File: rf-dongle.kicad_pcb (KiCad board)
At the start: 4 copper layers, 33 x 18 mm, 35 parts, among them J1 USB_A, J3 TC2030, SW1 SW_Push, SW2 SW_Push, U1 nRF52840-QIXX, X1 32MHz, X2 32.768kHz

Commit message: before new programming pins
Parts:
- added H1: VBUS, TestPoint:TestPoint_THTPad_D1.0mm_Drill0.5mm, F.Cu at (57.6, 41.6)
- added H2: VEXT, TestPoint:TestPoint_THTPad_D1.0mm_Drill0.5mm, F.Cu at (57.6, 44.6)
- added H3: SWDIO, TestPoint:TestPoint_THTPad_D1.0mm_Drill0.5mm, F.Cu at (57.6, 47.7)
- added H4: SWDCLK, TestPoint:TestPoint_THTPad_D1.0mm_Drill0.5mm, F.Cu at (57.6, 50.8)
- added H5: GND, TestPoint:TestPoint_THTPad_D1.0mm_Drill0.5mm, F.Cu at (57.8, 53.4)
- moved X1 0.08 mm to (46.5, 40.6)
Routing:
- net SWDIO: track 19.9 -> 20.5 mm
- net GND: track 26.6 -> 26.7 mm, vias 55 -> 54
- net D-: vias 1 -> 0
- net D+: vias 1 -> 0

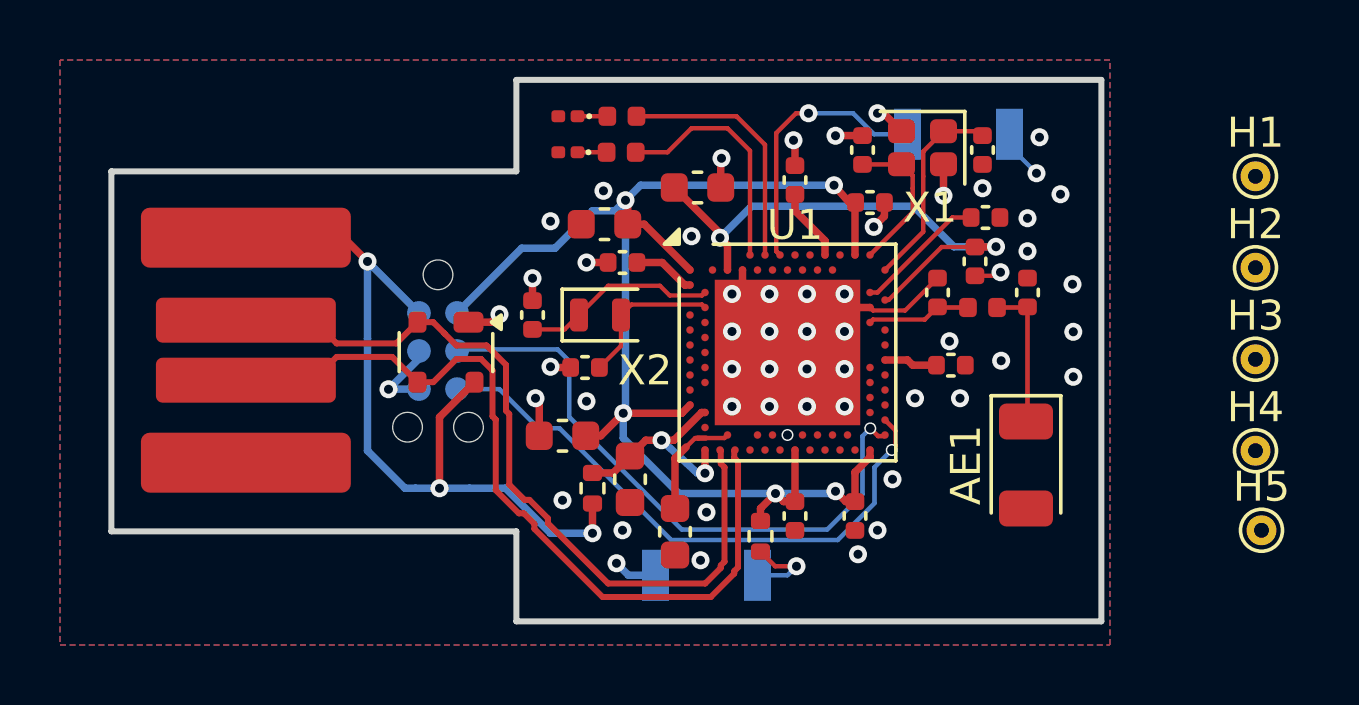
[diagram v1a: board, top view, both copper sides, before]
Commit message: rework programming pins, cleanup pcb routing
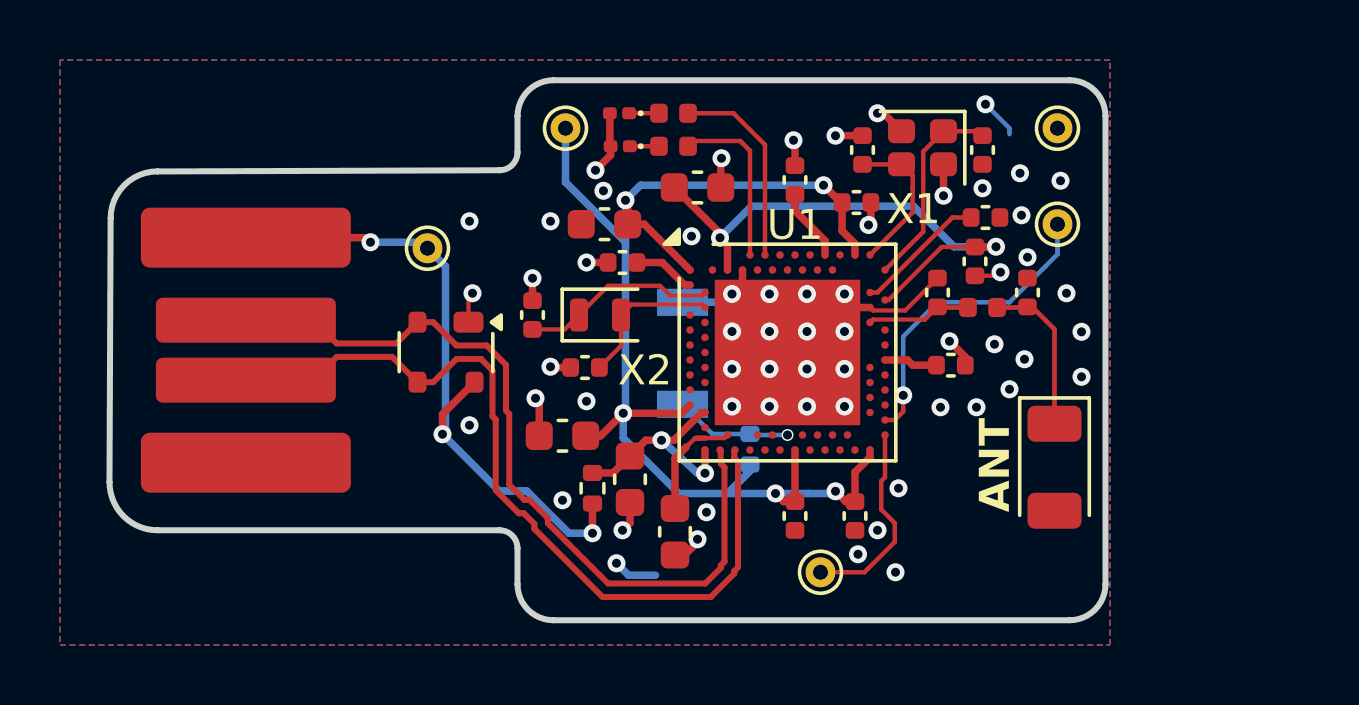
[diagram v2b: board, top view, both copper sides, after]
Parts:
- removed J3: TC2030, Connector:Tag-Connect_TC2030-IDC-NL_2x03_P1.27mm_Vertical
- removed SW2: SW_Push, Button_Switch_SMD:SW_SPST_B3U-1000P
- R2: moved to B.Cu
- moved H1 27.7 mm to (30.0, 44.0)
- moved H2 23.5 mm to (34.6, 40.0)
- moved H3 16.1 mm to (43.1, 54.8)
- moved H5 15.0 mm to (51.0, 40.0)
- moved H4 10.0 mm to (51.0, 43.2)
- moved SW1 7.44 mm to (38.5, 47.5), turned to -90 degrees
- moved R2 2.92 mm to (40.8, 50.7), turned to 90 degrees
- moved D3 1.76 mm to (38.2, 40.6)
- moved R4 1.76 mm to (36.4, 40.6)
- moved D2 1.72 mm to (38.2, 39.5)
- moved R3 1.72 mm to (36.4, 39.5)
- moved AE1 0.95 mm to (50.9, 51.3)
- moved C12 0.45 mm to (44.3, 42.5)
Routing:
- net SWDIO: track 20.5 -> 6.75 mm, vias 1 -> 0
- net BTN_1: track 9.06 -> 0.00 mm, vias 1 -> 0
- net SWDCLK: track 19.7 -> 10.7 mm
- net VBUS: track 26.8 -> 22.2 mm
- net RESET: track 8.15 -> 3.92 mm, vias 2 -> 1
- net GND: track 26.7 -> 30.3 mm, vias 54 -> 59
- net VEXT: track 46.8 -> 44.0 mm
- net LED_2: track 7.93 -> 5.75 mm
- net LED_1: track 8.35 -> 6.67 mm
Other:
- board size 33 x 18 mm -> 33.2 x 18 mm
- board text added: "ANT"
- board text added: "GND"
- board text added: "RESET"
- board text added: "SWDCLK"
- board text added: "SWDIO"
- board text added: "VBUS"
- board text added: "VEXT"

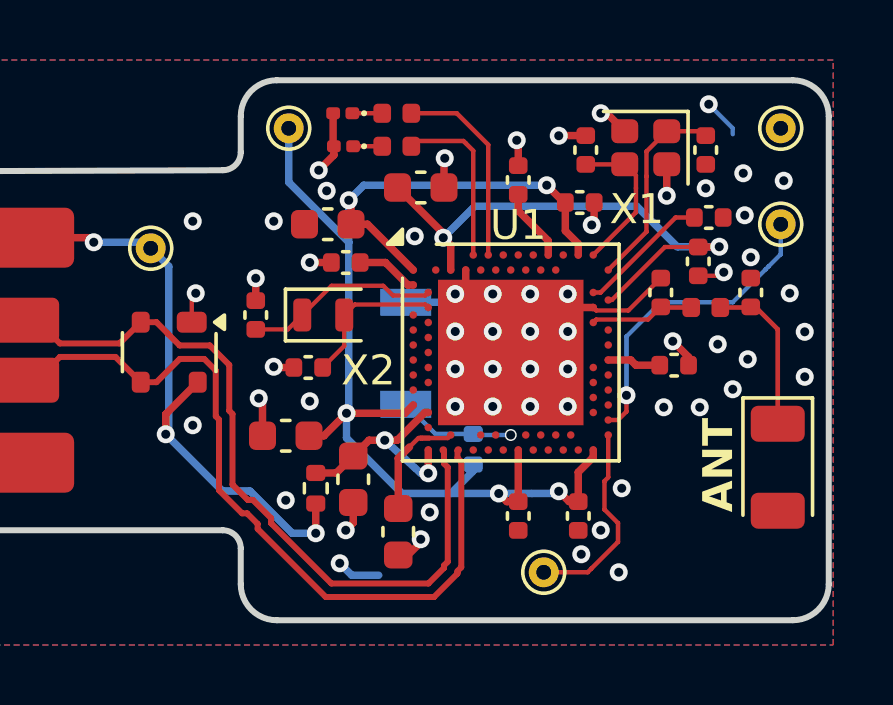
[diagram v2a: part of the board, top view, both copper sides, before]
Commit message: adjust footprints for handsoldering, tweak antenna
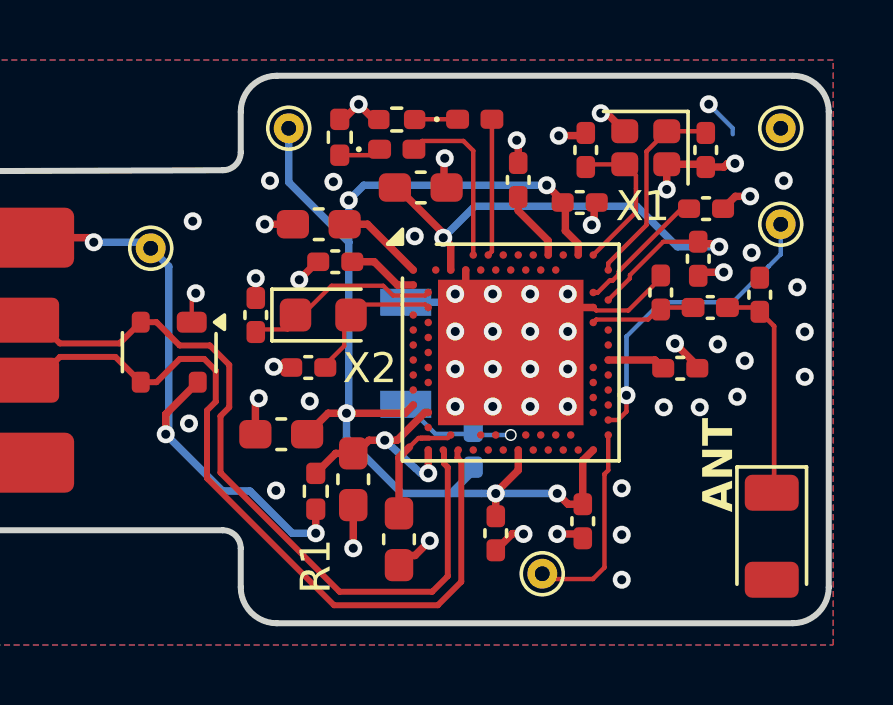
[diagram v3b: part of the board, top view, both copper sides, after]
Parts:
- C1, C10, C11, C12, C13, C17, C18, C2, C3, C4, C5, C7, C8, C9: footprint Capacitor_SMD:C_0402_1005Metric -> Capacitor_SMD:C_0402_1005Metric_Pad0.74x0.62mm_HandSolder
- C14, C15, C19, C20, C6: footprint Capacitor_SMD:C_0603_1608Metric -> Capacitor_SMD:C_0603_1608Metric_Pad1.08x0.95mm_HandSolder
- D2, D3: footprint LED_SMD:LED_0402_1005Metric -> LED_SMD:LED_0402_1005Metric_Pad0.77x0.64mm_HandSolder
- L1: footprint Inductor_SMD:L_0402_1005Metric -> Inductor_SMD:L_0402_1005Metric_Pad0.77x0.64mm_HandSolder
- R1, R2: footprint Resistor_SMD:R_0402_1005Metric -> Resistor_SMD:R_0402_1005Metric_Pad0.72x0.64mm_HandSolder
- R3, R4: footprint Resistor_SMD:R_0201_0603Metric -> Resistor_SMD:R_0402_1005Metric_Pad0.72x0.64mm_HandSolder
- U1: value nRF52840-QIXX -> NRF52840-QIAA-R7
- X2: footprint Crystal:Crystal_SMD_2012-2Pin_2.0x1.2mm -> Crystal:Crystal_SMD_2012-2Pin_2.0x1.2mm_HandSoldering
- moved D2 2.61 mm to (40.8, 39.7)
- moved AE1 2.31 mm to (50.7, 53.6)
- moved R3 1.81 mm to (38.2, 39.7)
- moved C7 0.95 mm to (41.5, 53.5)
- moved C5 0.35 mm to (36.1, 44.5)
- moved R4 0.33 mm to (36.3, 40.3), turned to -90 degrees
- moved C4 0.31 mm to (50.3, 45.5)
- moved C11 0.31 mm to (48.5, 42.7)
- moved C14 0.30 mm to (35.6, 43.2)
- moved C20 0.25 mm to (38.3, 53.7)
- moved C8 0.23 mm to (44.4, 53.1)
- moved C9 0.23 mm to (47.6, 48.0)
- moved C6 0.16 mm to (34.4, 50.2)
- moved L1 0.15 mm to (48.6, 46.0)
- moved D3 0.10 mm to (38.2, 40.7)
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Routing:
- net GND: track 30.3 -> 35.9 mm, vias 59 -> 58
- net /RF: track 5.05 -> 7.42 mm
- net LED_1: track 6.67 -> 4.58 mm
- net D+: track 27.5 -> 28.1 mm
- net D-: track 26.7 -> 27.3 mm
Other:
- board size 33.2 x 18 mm -> 33.2 x 18.2 mm
- board text added: "1.6mm feed track in keepout area"
- board text added: "ANTENNA footprint"
- board text added: "Keepout"

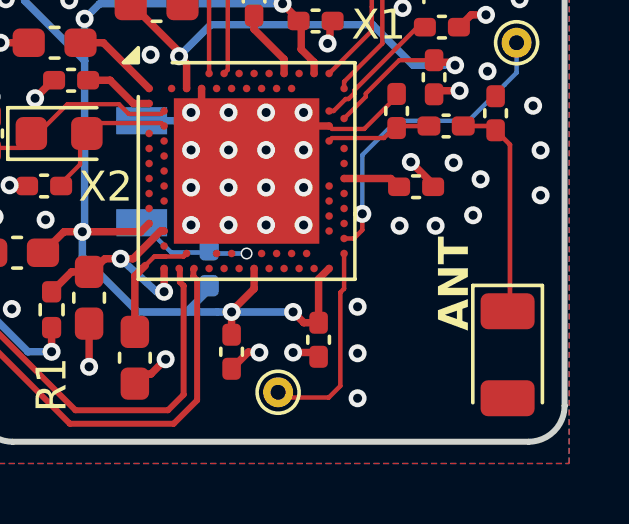
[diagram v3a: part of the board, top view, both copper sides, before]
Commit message: adjust silkscreen
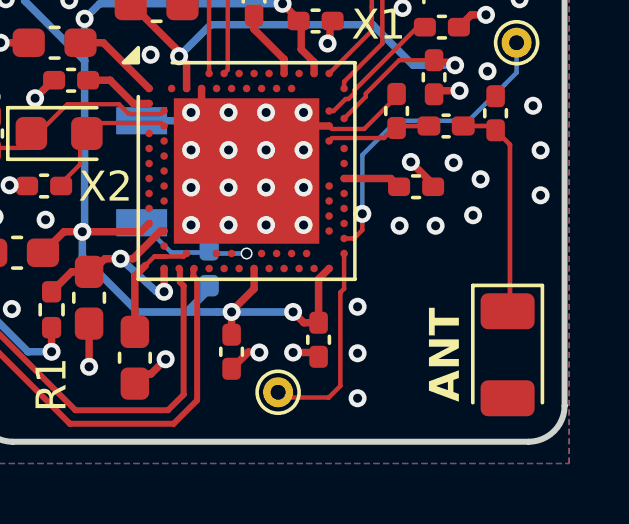
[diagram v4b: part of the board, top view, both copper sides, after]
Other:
- board text added: "nglgzz"
- board text added: "rev1"
- board text added: "rf-dongle"
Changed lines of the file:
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@@
 			(at 0 1.55 270)
 			(layer "B.SilkS")
+			(hide yes)
 			(effects
 				(font
@@
 			(at 0 -1.17 270)
 			(layer "B.Fab")
+			(hide yes)
 			(effects
 				(font
@@
 	)
 	(gr_text "ANT"
-		(at 49.5 52.8 90)
+		(at 49.2 53.6 90)
 		(layer "F.SilkS")
 		(effects
@@
 				(bold yes)
 			)
-			(justify left bottom)
+			(justify bottom)
 		)
 	)
@@
 		)
 	)
+	(gr_text "rev1"
+		(at 23.3 49.95 0)
+		(layer "B.SilkS" knockout)
+		(effects
+			(font
+				(size 1 1)
+				(thickness 0.2)
+				(bold yes)
+			)
+			(justify left bottom mirror)
+		)
+	)
 	(gr_text "SWDCLK"
 		(at 49.6 43.2 0)
@@
 		)
 	)
+	(gr_text "nglgzz"
+		(at 19.9 46.65 0)
+		(layer "B.SilkS")
+		(effects
+			(font
+				(size 1 1)
+				(thickness 0.2)
+				(bold yes)
+			)
+			(justify right bottom mirror)
+		)
+	)
+	(gr_text "rf-dongle"
+		(at 19.85 48.1 0)
+		(layer "B.SilkS")
+		(effects
+			(font
+				(size 1 1)
+				(thickness 0.2)
+				(bold yes)
+			)
+			(justify right bottom mirror)
+		)
+	)

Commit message: ordered rev 1
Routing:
- net VEXT: track 43.7 -> 44.7 mm
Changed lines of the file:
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@@
 	)
 	(segment
-		(start 45.2 39.5)
+		(start 45.8 39.2)
 		(end 45.8 40.1)
 		(width 0.25)
@@
 	)
 	(segment
-		(start 45 39.5)
-		(end 45.2 39.5)
-		(width 0.25)
-		(layer "F.Cu")
-		(net 2)
-	)
-	(segment
 		(start 49.98 42.27)
 		(end 49.4875 42.27)
@@
 	)
 	(via
-		(at 45 39.5)
+		(at 45.8 39.2)
 		(size 0.6)
 		(drill 0.3)
@@
 	)
 	(via
-		(at 36.087851 41.785421)
-		(size 0.6)
-		(drill 0.3)
-		(layers "F.Cu" "B.Cu")
-		(free yes)
-		(net 2)
-	)
-	(via
 		(at 49.475 41.175)
 		(size 0.6)
@@
 	)
 	(via
+		(at 35.8 42)
+		(size 0.6)
+		(drill 0.3)
+		(layers "F.Cu" "B.Cu")
+		(net 2)
+	)
+	(via
 		(at 47.1 49.3)
 		(size 0.6)
@@
 	)
 	(via
-		(at 48.6 39.2)
+		(at 49.5 39.2)
 		(size 0.6)
 		(drill 0.3)
@@
 		(layers "F.Cu" "B.Cu")
 		(free yes)
+		(net 2)
+	)
+	(segment
+		(start 49.4 39.3)
+		(end 49.4 40.2)
+		(width 0.145)
+		(layer "B.Cu")
 		(net 2)
 	)
@@
 	)
 	(segment
-		(start 49.4 40)
-		(end 49.4 40.2)
-		(width 0.145)
-		(layer "B.Cu")
-		(net 2)
-	)
-	(segment
-		(start 48.6 39.2)
-		(end 49.4 40)
+		(start 49.5 39.2)
+		(end 49.4 39.3)
 		(width 0.145)
 		(layer "B.Cu")
@@
 	)
 	(segment
+		(start 36.4625 42.457775)
+		(end 36.4625 43.2)
+		(width 0.25)
+		(layer "F.Cu")
+		(net 5)
+	)
+	(segment
 		(start 38.475 49.5)
 		(end 38.75 49.225)
@@
 	)
 	(segment
-		(start 36.675 42.475)
-		(end 36.6 42.4)
+		(start 36.660138 42.260138)
+		(end 36.4625 42.457775)
 		(width 0.25)
 		(layer "F.Cu")
@@
 	)
 	(via
-		(at 36.6 42.4)
+		(at 36.660138 42.260138)
 		(size 0.6)
 		(drill 0.3)
@@
 	)
 	(segment
+		(start 36.660138 42.260138)
+		(end 36.825709 42.094567)
+		(width 0.25)
+		(layer "B.Cu")
+		(net 5)
+	)
+	(segment
 		(start 36.525 50.325)
 		(end 38.3 52.1)
@@
 	)
 	(segment
-		(start 37.1 41.9)
-		(end 36.6 42.4)
-		(width 0.25)
-		(layer "B.Cu")
-		(net 5)
-	)
-	(segment
 		(start 36.525 49.5)
 		(end 36.525 49.375)
@@
 	)
 	(segment
+		(start 36.905433 42.094567)
+		(end 37.1 41.9)
+		(width 0.25)
+		(layer "B.Cu")
+		(net 5)
+	)
+	(segment
 		(start 34.6 40)
 		(end 34.6 41.8)
@@
 	)
 	(segment
+		(start 37.1 41.9)
+		(end 43.2 41.9)
+		(width 0.25)
+		(layer "B.Cu")
+		(net 5)
+	)
+	(segment
 		(start 36.6 49.3)
 		(end 36.6 43.8)
@@
 	)
 	(segment
-		(start 43.2 41.9)
-		(end 37.1 41.9)
+		(start 36.825709 42.094567)
+		(end 36.905433 42.094567)
+		(width 0.25)
+		(layer "B.Cu")
+		(net 5)
+	)
+	(segment
+		(start 36.6 42.320275)
+		(end 36.6 43.8)
+		(width 0.25)
+		(layer "B.Cu")
+		(net 5)
+	)
+	(segment
+		(start 36.660138 42.260138)
+		(end 36.6 42.320275)
 		(width 0.25)
 		(layer "B.Cu")
@@
 		(width 0.25)
 		(layer "B.Cu")
-		(net 5)
-	)
-	(segment
-		(start 36.6 43.8)
-		(end 36.6 42.4)
-		(width 0.25)
-		(layer "B.Cu")

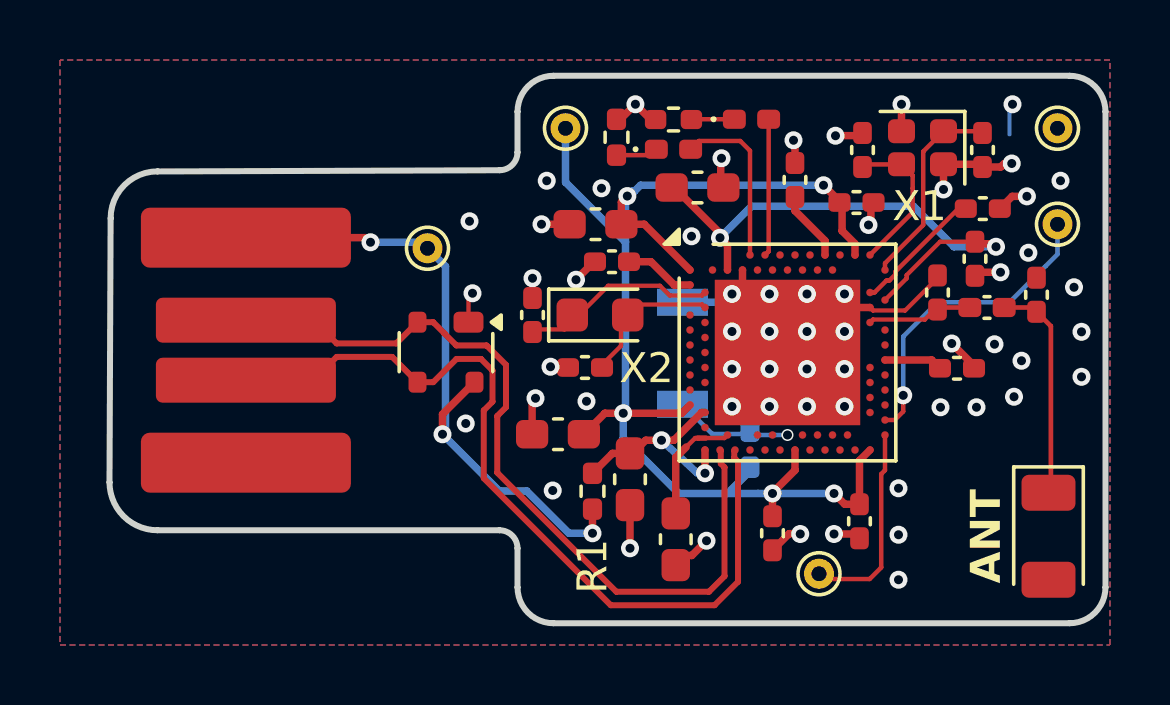
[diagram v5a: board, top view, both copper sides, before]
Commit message: reverse USB pads and remove unnecessary component
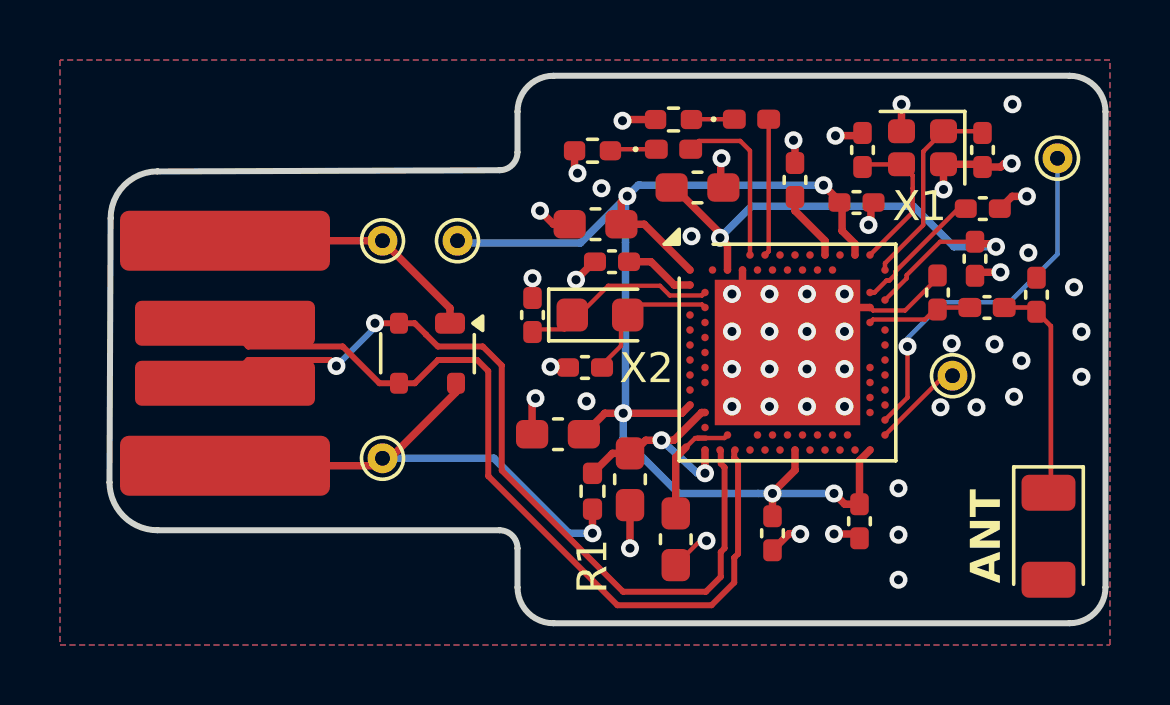
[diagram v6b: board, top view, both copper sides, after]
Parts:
- removed C9: 820pF, Capacitor_SMD:C_0402_1005Metric_Pad0.74x0.62mm_HandSolder
- removed R2: 10k, Resistor_SMD:R_0402_1005Metric_Pad0.72x0.64mm_HandSolder
- removed SW1: SW_Push, Button_Switch_SMD:SW_SPST_B3U-1000P
- moved H5 22.8 mm to (28.5, 43.8)
- moved H3 7.96 mm to (47.5, 48.2)
- moved H1 7.16 mm to (28.5, 51.0)
- moved H2 5.20 mm to (31.0, 43.8)
- moved H4 2.20 mm to (51.0, 41.0)
- moved R4 0.92 mm to (35.5, 40.8), turned to 0 degrees
- moved J1 0.70 mm to (23.2, 47.5)
- moved D1 0.62 mm to (30.0, 47.5)
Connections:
- U1 pad A12: BTN_1 -> unconnected-(U1-P0.02-PadA12)
- U1 pad AC13: RESET -> unconnected-(U1-~{RESET}-PadAC13)
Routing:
- net GND: track 35.4 -> 40.1 mm, vias 58 -> 53
- net VBUS: track 22.2 -> 17.8 mm, vias 3 -> 1
- net RESET: track 3.92 -> 0.00 mm, vias 1 -> 0
- net SWDIO: track 6.83 -> 3.07 mm
- net /DEC5: track 1.95 -> 0.00 mm
- net SWDCLK: track 10.7 -> 12.4 mm
- net D-: track 27.3 -> 27.9 mm, vias 0 -> 2
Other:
- board text added: "rev3"
- board text removed: "#808080D4"
- board text removed: "0"
- board text removed: "0 mm"
- board text removed: "0.01 mm"
- board text removed: "0.0152 mm"
- board text removed: "0.02"
- board text removed: "0.035 mm"
- board text removed: "0.0994 mm"
- board text removed: "1"
- board text removed: "1.265 mm"
- board text removed: "3.3"
- board text removed: "4.1"
- board text removed: "4.5"
- board text removed: "B.Cu"
- board text removed: "B.Mask"
- board text removed: "B.Paste"
- board text removed: "B.Silkscreen"
- board text removed: "Bottom Silk Screen"
- board text removed: "Bottom Solder Mask"
- board text removed: "Bottom Solder Paste"
- board text removed: "Color"
- board text removed: "Dielectric"
- board text removed: "Epsilon R"
- board text removed: "F.Cu"
- board text removed: "F.Mask"
- board text removed: "F.Paste"
- board text removed: "F.Silkscreen"
- board text removed: "FR4"
- board text removed: "In1.Cu"
- board text removed: "In2.Cu"
- board text removed: "Layer Name"
- board text removed: "Loss Tangent"
- board text removed: "Material"
- board text removed: "Not specified"
- board text removed: "RESET"
- board text removed: "Thickness (mm)"
- board text removed: "Top Silk Screen"
- board text removed: "Top Solder Mask"
- board text removed: "Top Solder Paste"
- board text removed: "Type"
- board text removed: "copper"
- board text removed: "core"
- board text removed: "prepreg"
- board text removed: "rev1"
